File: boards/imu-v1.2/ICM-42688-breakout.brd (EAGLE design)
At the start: 15.2 x 12.7 mm, 7 parts, among them U3 ICM-42688ICM42688

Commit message: Design Review Feedback Changes
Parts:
- R1: value 100 -> 330
- moved D1 1.00 mm to (3.60, -1.20)
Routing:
- net N$1: track 1.81 -> 2.81 mm
- net GND: track 9.59 -> 10.1 mm
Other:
- board text added: "42605"
- board text added: "42688"
- board text added: "Feb. 2022"
- board text added: "IMU Breakout v1.2"
- board text removed: "2021"
- board text removed: ">VERSION"
- board text removed: "ICM 42688"
- board text removed: "IMU Breakout"

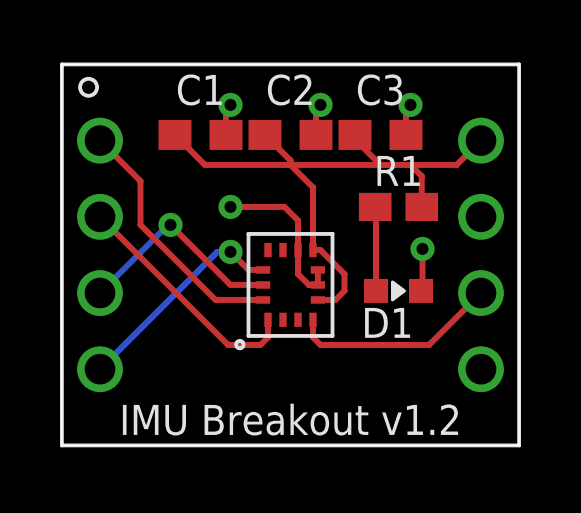
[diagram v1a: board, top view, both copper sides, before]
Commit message: Design Review Fixes
Fixed the comments from the design review on 02/12/22
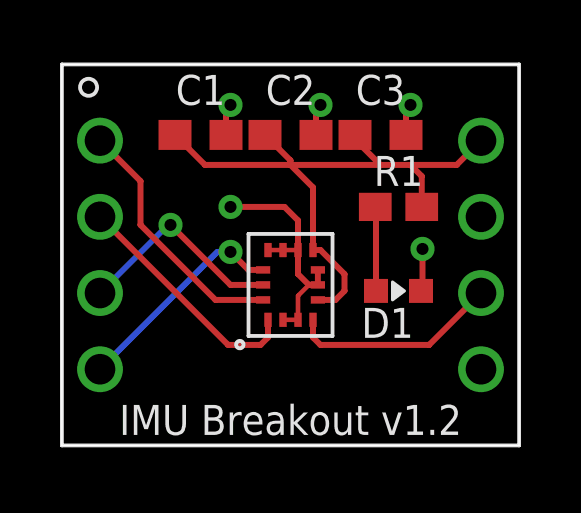
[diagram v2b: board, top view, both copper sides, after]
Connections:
- net GND: now also U3.P$10, U3.P$11, U3.P$2, U3.P$3
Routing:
- net GND: track 10.1 -> 13.0 mm
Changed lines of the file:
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@@
 <layer number="14" name="Route14" color="22" fill="1" visible="no" active="no"/>
 <layer number="15" name="Route15" color="23" fill="1" visible="no" active="no"/>
-<layer number="16" name="Bottom" color="1" fill="1" visible="no" active="yes"/>
+<layer number="16" name="Bottom" color="1" fill="1" visible="yes" active="yes"/>
 <layer number="17" name="Pads" color="2" fill="1" visible="yes" active="yes"/>
 <layer number="18" name="Vias" color="2" fill="1" visible="yes" active="yes"/>
@@
 <wire x1="-7.62" y1="6.35" x2="-7.62" y2="-6.35" width="0" layer="20"/>
 <text x="0" y="-5" size="1" layer="21" font="vector" ratio="15" rot="R180" align="bottom-center">IMU Breakout v1.2</text>
-<text x="0" y="2" size="1.5" layer="22" font="vector" ratio="15" rot="MR0" align="bottom-center">Feb. 2022</text>
+<text x="0" y="2.8" size="1.5" layer="22" font="vector" ratio="15" rot="MR0" align="bottom-center">Feb. 2022</text>
 <text x="2.2" y="-2.3" size="1" layer="22" font="vector" ratio="15" rot="MR0" align="bottom-center">42605</text>
 <text x="2.2" y="-5.3" size="1" layer="22" font="vector" ratio="15" rot="MR0" align="bottom-center">42688</text>
@@
 <wire x1="-0.2" y1="1.6" x2="0.25" y2="1.15" width="0.2" layer="1"/>
 <wire x1="0.25" y1="1.15" x2="0.25" y2="0.1625" width="0.2" layer="1"/>
+<contactref element="U3" pad="P$2"/>
+<contactref element="U3" pad="P$3"/>
+<contactref element="U3" pad="P$10"/>
+<contactref element="U3" pad="P$11"/>
+<wire x1="-0.25" y1="-2.1625" x2="0.25" y2="-2.1625" width="0.1524" layer="1"/>
+<wire x1="0.25" y1="-2.1625" x2="0.25" y2="-1.3625" width="0.1524" layer="1"/>
+<wire x1="0.25" y1="-1.3625" x2="0.6125" y2="-1" width="0.1524" layer="1"/>
+<wire x1="0.25" y1="0.1625" x2="-0.25" y2="0.1625" width="0.1524" layer="1"/>
+<wire x1="-0.25" y1="0.1625" x2="-0.75" y2="0.1625" width="0.1524" layer="1"/>
 </signal>
 <signal name="+3.3V">

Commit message: Update ICM-42688-breakout.brd
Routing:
- net GND: track 13.0 -> 15.0 mm
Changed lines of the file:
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@@
 </class>
 </classes>
-<designrules name="RJ2LayerDRU">
-<description language="en">&lt;b&gt;EAGLE Design Rules&lt;/b&gt;
+<designrules name="JLCPCB (2 Layer)">
+<description language="en">&lt;b&gt;JLCPCB Design Rules (2 Layers)&lt;/b&gt;
 &lt;p&gt;
 The default Design Rules have been set to cover
-a wide range of applications. Your particular design
-may have different requirements, so please make the
-necessary adjustments and save your customized
-design rules under a new name.</description>
-<param name="layerSetup" value="(1*16)"/>
-<param name="mtCopper" value="0.0356mm 0.035mm 0.035mm 0.035mm 0.035mm 0.035mm 0.035mm 0.035mm 0.035mm 0.035mm 0.035mm 0.035mm 0.035mm 0.035mm 0.035mm 0.0356mm"/>
-<param name="mtIsolate" value="63mil 0.15mm 0.2mm 0.15mm 0.2mm 0.15mm 0.2mm 0.15mm 0.2mm 0.15mm 0.2mm 0.15mm 0.2mm 0.15mm 0.2mm"/>
-<param name="mdWireWire" value="6mil"/>
-<param name="mdWirePad" value="6mil"/>
-<param name="mdWireVia" value="6mil"/>
-<param name="mdPadPad" value="6mil"/>
-<param name="mdPadVia" value="6mil"/>
-<param name="mdViaVia" value="6mil"/>
-<param name="mdSmdPad" value="6mil"/>
-<param name="mdSmdVia" value="0mil"/>
-<param name="mdSmdSmd" value="6mil"/>
-<param name="mdViaViaSameLayer" value="8mil"/>
+a wide range of applications.
+&lt;p&gt;
+Source: &lt;a href=&quot;https://jlcpcb.com/capabilities/Capabilities&quot;&gt;JLCPCB&lt;/a&gt;
+&lt;/p&gt;</description>
+<param name="layerSetup" value="(1+16)"/>
+<param name="mtCopper" value="0.035mm 0.035mm 0.035mm 0.035mm 0.035mm 0.035mm 0.035mm 0.035mm 0.035mm 0.035mm 0.035mm 0.035mm 0.035mm 0.035mm 0.035mm 0.035mm"/>
+<param name="mtIsolate" value="1.53mm 0.15mm 0.2mm 0.15mm 0.2mm 0.15mm 0.2mm 0.15mm 0.2mm 0.15mm 0.2mm 0.15mm 0.2mm 0.15mm 0.2mm"/>
+<param name="mdWireWire" value="5mil"/>
+<param name="mdWirePad" value="5mil"/>
+<param name="mdWireVia" value="8mil"/>
+<param name="mdPadPad" value="5mil"/>
+<param name="mdPadVia" value="10mil"/>
+<param name="mdViaVia" value="20mil"/>
+<param name="mdSmdPad" value="5mil"/>
+<param name="mdSmdVia" value="10mil"/>
+<param name="mdSmdSmd" value="5mil"/>
+<param name="mdViaViaSameLayer" value="6mil"/>
 <param name="mnLayersViaInSmd" value="2"/>
-<param name="mdCopperDimension" value="0mil"/>
-<param name="mdDrill" value="6mil"/>
+<param name="mdCopperDimension" value="0.2mm"/>
+<param name="mdDrill" value="21mil"/>
 <param name="mdSmdStop" value="0mil"/>
-<param name="msWidth" value="6mil"/>
-<param name="msDrill" value="15mil"/>
+<param name="msWidth" value="5mil"/>
+<param name="msDrill" value="0.3mm"/>
 <param name="msMicroVia" value="9.99mm"/>
 <param name="msBlindViaRatio" value="0.5"/>
@@
 <param name="rvViaOuter" value="0.25"/>
 <param name="rvViaInner" value="0.25"/>
-<param name="rvMicroViaOuter" value="0.25"/>
-<param name="rvMicroViaInner" value="0.25"/>
-<param name="rlMinPadTop" value="10mil"/>
+<param name="rvMicroViaOuter" value="0"/>
+<param name="rvMicroViaInner" value="0"/>
+<param name="rlMinPadTop" value="6mil"/>
 <param name="rlMaxPadTop" value="20mil"/>
-<param name="rlMinPadInner" value="10mil"/>
+<param name="rlMinPadInner" value="6mil"/>
 <param name="rlMaxPadInner" value="20mil"/>
-<param name="rlMinPadBottom" value="10mil"/>
+<param name="rlMinPadBottom" value="6mil"/>
 <param name="rlMaxPadBottom" value="20mil"/>
-<param name="rlMinViaOuter" value="8mil"/>
-<param name="rlMaxViaOuter" value="20mil"/>
-<param name="rlMinViaInner" value="8mil"/>
-<param name="rlMaxViaInner" value="20mil"/>
-<param name="rlMinMicroViaOuter" value="4mil"/>
+<param name="rlMinViaOuter" value="6mil"/>
+<param name="rlMaxViaOuter" value="12mil"/>
+<param name="rlMinViaInner" value="6mil"/>
+<param name="rlMaxViaInner" value="12mil"/>
+<param name="rlMinMicroViaOuter" value="6mil"/>
 <param name="rlMaxMicroViaOuter" value="20mil"/>
-<param name="rlMinMicroViaInner" value="4mil"/>
+<param name="rlMinMicroViaInner" value="6mil"/>
 <param name="rlMaxMicroViaInner" value="20mil"/>
 <param name="psTop" value="-1"/>
@@
 <param name="mvStopFrame" value="1"/>
 <param name="mvCreamFrame" value="0"/>
-<param name="mlMinStopFrame" value="4mil"/>
-<param name="mlMaxStopFrame" value="4mil"/>
+<param name="mlMinStopFrame" value="2mil"/>
+<param name="mlMaxStopFrame" value="2mil"/>
 <param name="mlMinCreamFrame" value="0mil"/>
 <param name="mlMaxCreamFrame" value="0mil"/>
-<param name="mlViaStopLimit" value="0mil"/>
+<param name="mlViaStopLimit" value="30mil"/>
 <param name="srRoundness" value="0"/>
 <param name="srMinRoundness" value="0mil"/>
@@
 <via x="-2" y="1.6" extent="1-16" drill="0.4"/>
 <wire x1="-2" y1="1.6" x2="-0.2" y2="1.6" width="0.2" layer="1"/>
-<wire x1="3.85" y1="4" x2="3.85" y2="4.85" width="0.2" layer="1"/>
-<wire x1="3.85" y1="4.85" x2="4" y2="5" width="0.2" layer="1"/>
-<via x="4" y="5" extent="1-16" drill="0.4"/>
-<wire x1="0.85" y1="4" x2="0.85" y2="4.85" width="0.2" layer="1"/>
-<wire x1="0.85" y1="4.85" x2="1" y2="5" width="0.2" layer="1"/>
-<via x="1" y="5" extent="1-16" drill="0.4"/>
-<wire x1="-2.15" y1="4" x2="-2.15" y2="4.85" width="0.2" layer="1"/>
-<wire x1="-2.15" y1="4.85" x2="-2" y2="5" width="0.2" layer="1"/>
-<via x="-2" y="5" extent="1-16" drill="0.4"/>
+<wire x1="4.6" y1="5.5" x2="3.85" y2="4.75" width="0.2" layer="1"/>
+<wire x1="3.85" y1="4" x2="3.85" y2="4.75" width="0.2" layer="1"/>
+<via x="4.6" y="5.5" extent="1-16" drill="0.4"/>
+<wire x1="0.85" y1="4" x2="0.85" y2="5.15" width="0.2" layer="1"/>
+<wire x1="0.85" y1="5.15" x2="1.3" y2="5.6" width="0.2" layer="1"/>
+<via x="1.3" y="5.6" extent="1-16" drill="0.4"/>
+<wire x1="-2.15" y1="4" x2="-2.15" y2="5.15" width="0.2" layer="1"/>
+<wire x1="-2.15" y1="5.15" x2="-1.8" y2="5.5" width="0.2" layer="1"/>
+<via x="-1.8" y="5.5" extent="1-16" drill="0.4"/>
 <contactref element="D1" pad="C"/>
 <via x="4.4" y="0.2" extent="1-16" drill="0.4"/>

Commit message: final revision changes
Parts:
- added U$1: (no value), RoboJackets-Aesthetics:ROBOBUZZ_0.2X
- moved U3 1.00 mm to (0.00, 0.00)
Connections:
- net GND: now also KIT1.7
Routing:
- net INT: track 7.01 -> 6.11 mm
- net GND: track 15.0 -> 14.2 mm
- net MISO: track 8.06 -> 7.30 mm
- net +3.3V: track 21.3 -> 20.7 mm
- added copper zone on layer 1, net GND
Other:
- board text added: "IMU Breakout v2.0"
- board text added: "RoboJackets Feb. 2022"
- board text removed: "Feb. 2022"
- board text removed: "IMU Breakout v1.2"
